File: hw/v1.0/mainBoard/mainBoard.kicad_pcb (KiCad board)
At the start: 2 copper layers, 50 x 100 mm, 124 parts, among them J10 BAT+, J15 U.FL, J4 PROGRAMMER, J6 EN_3V3_PROGRAMMER, J8 PMS5003, J9 BAT-, Q1 MMBT3904, Q10 AO3401A, Q11 2N7002, Q12 AO3401A, Q13 2N7002, Q14 AO3401A, Q15 2N7002, Q2 MMBT3904, Q3 AO3401A, Q4 2N7002, Q5 AO3401A, Q6 2N7002, Q7 2N7002, Q8 2N7002, Q9 AO3401A, SW1 PWR_ON, SW2 PWR_OFF, SW3 RESET, SW4 SW_Push, U1 ESP32-WROOM-32, U10 AP1603, U11 NCP115ASN180T2G, U2 MCP3202-BI/SN, U3 AMS1117-3.3, U4 VEML7700, U5 RFM95W-868S2, U6 ML8511, U7 BMP388, U8 SGP30, U9 SHT40

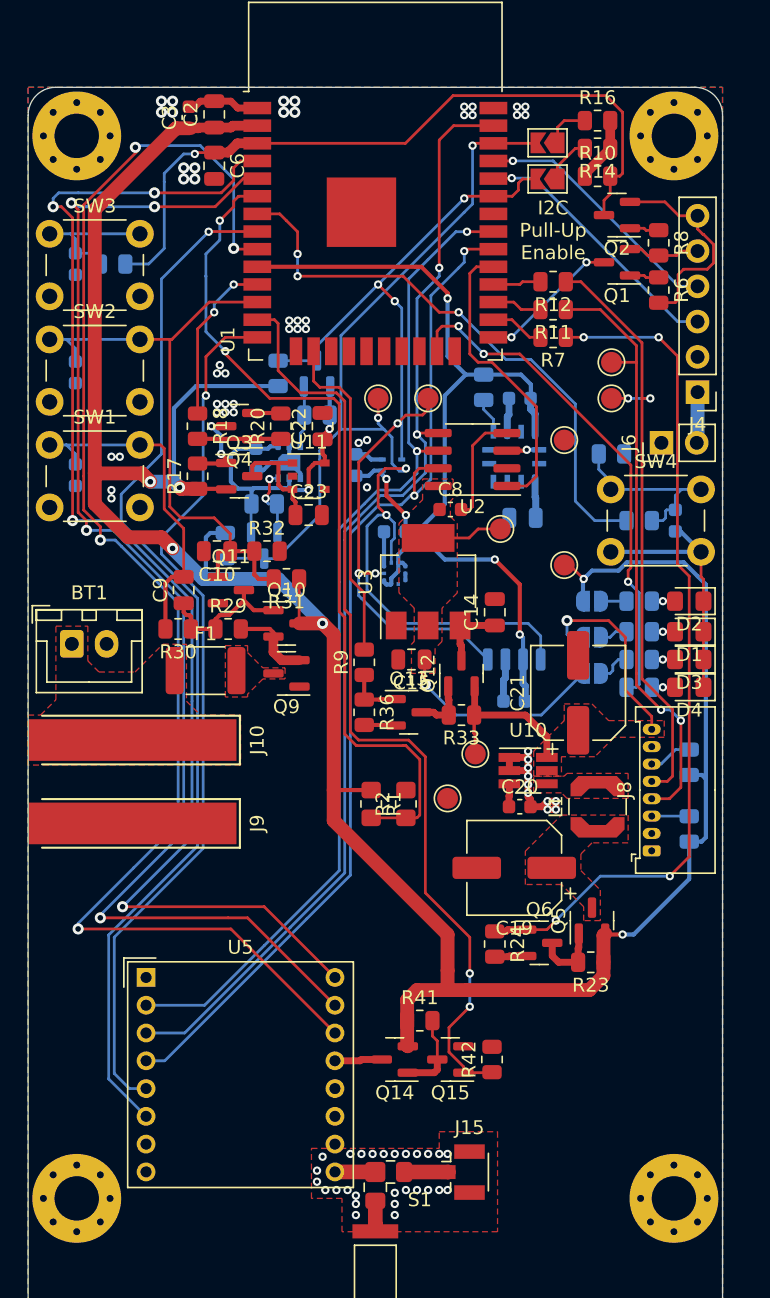
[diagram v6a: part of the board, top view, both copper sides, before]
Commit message: Tweak silkscreen at mainBoard, add MPPT option to batteryCharger
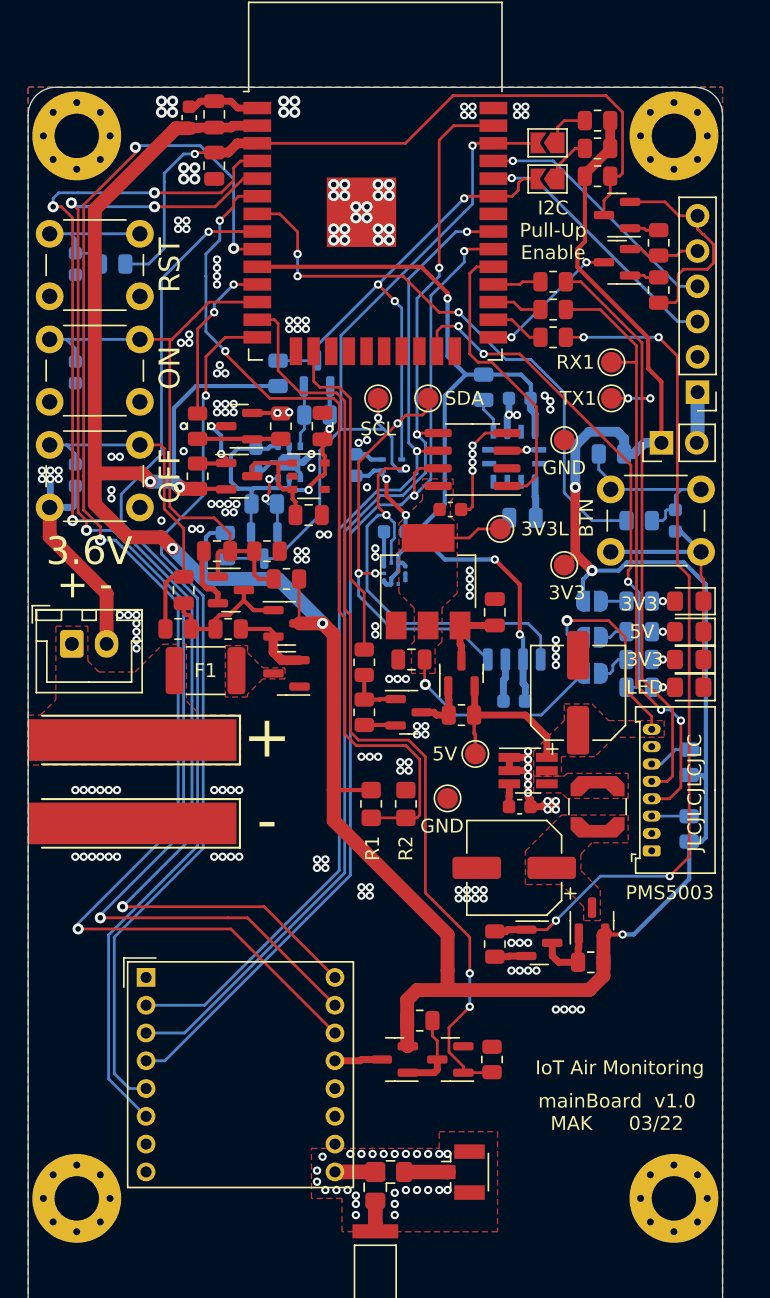
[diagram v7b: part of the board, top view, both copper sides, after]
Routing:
- net 3V3: track 192.0 -> 230.6 mm, vias 6 -> 7
- net GND: track 66.6 -> 89.9 mm, vias 79 -> 226
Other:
- board text added: "+"
- board text added: "-"
- board text added: "3.6V"
- board text added: "3V3"
- board text added: "3V3L"
- board text added: "5V"
- board text added: "BTN"
- board text added: "DTR"
- board text added: "EN 3V3"
- board text added: "EN PWR LEDS"
- board text added: "GND"
- board text added: "IoT Air Monitoring"
- board text added: "JLCJLCJLCJLC"
- board text added: "LED"
- board text added: "OFF"
- board text added: "ON"
- board text added: "PMS5003"
- board text added: "PROGRAMMER"
- board text added: "RST"
- board text added: "RTS"
- board text added: "RX"
- board text added: "RX1"
- board text added: "SCL"
- board text added: "SDA"
- board text added: "TX"
- board text added: "TX1"
- board text added: "mainBoard v1.0 MAK 03/22"
